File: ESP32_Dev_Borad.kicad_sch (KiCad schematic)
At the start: 33 parts, among them J1 USB_B_Micro, J2 Conn_01x19_Pin, J3 Conn_01x19_Pin, Q1 MMSS8050-H-TP, Q2 MMSS8050-H-TP, SW1 SW_Push, SW2 SW_Push, U1 CP2102N-A01-GQFN28, U2 AMS1117-3.3

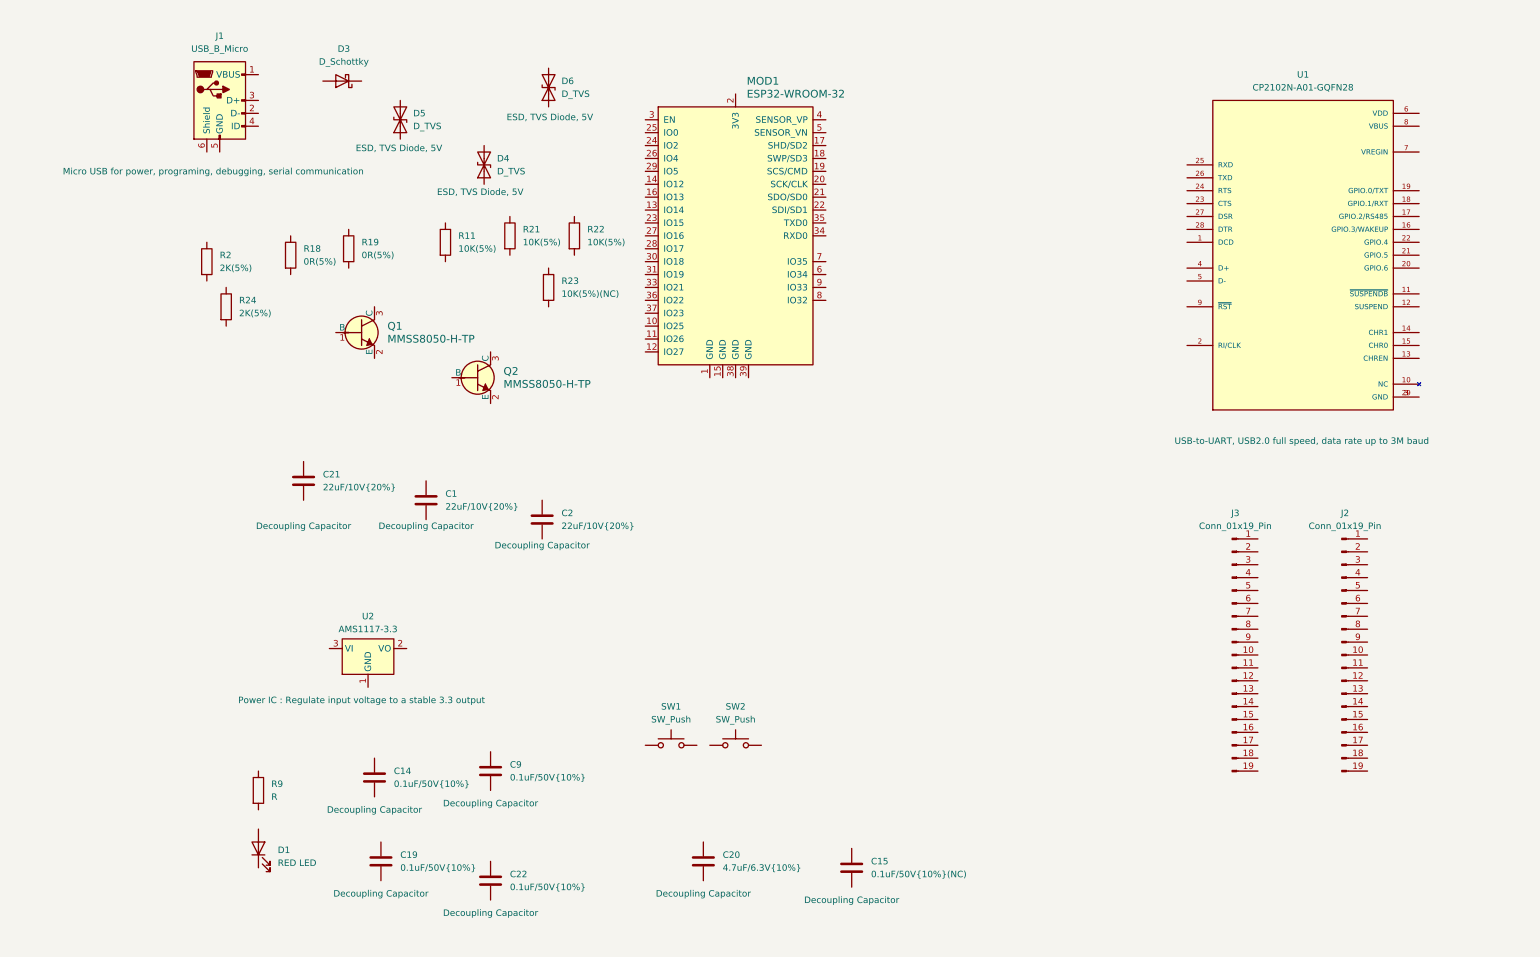
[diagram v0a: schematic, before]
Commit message: Done Arranging the schematic
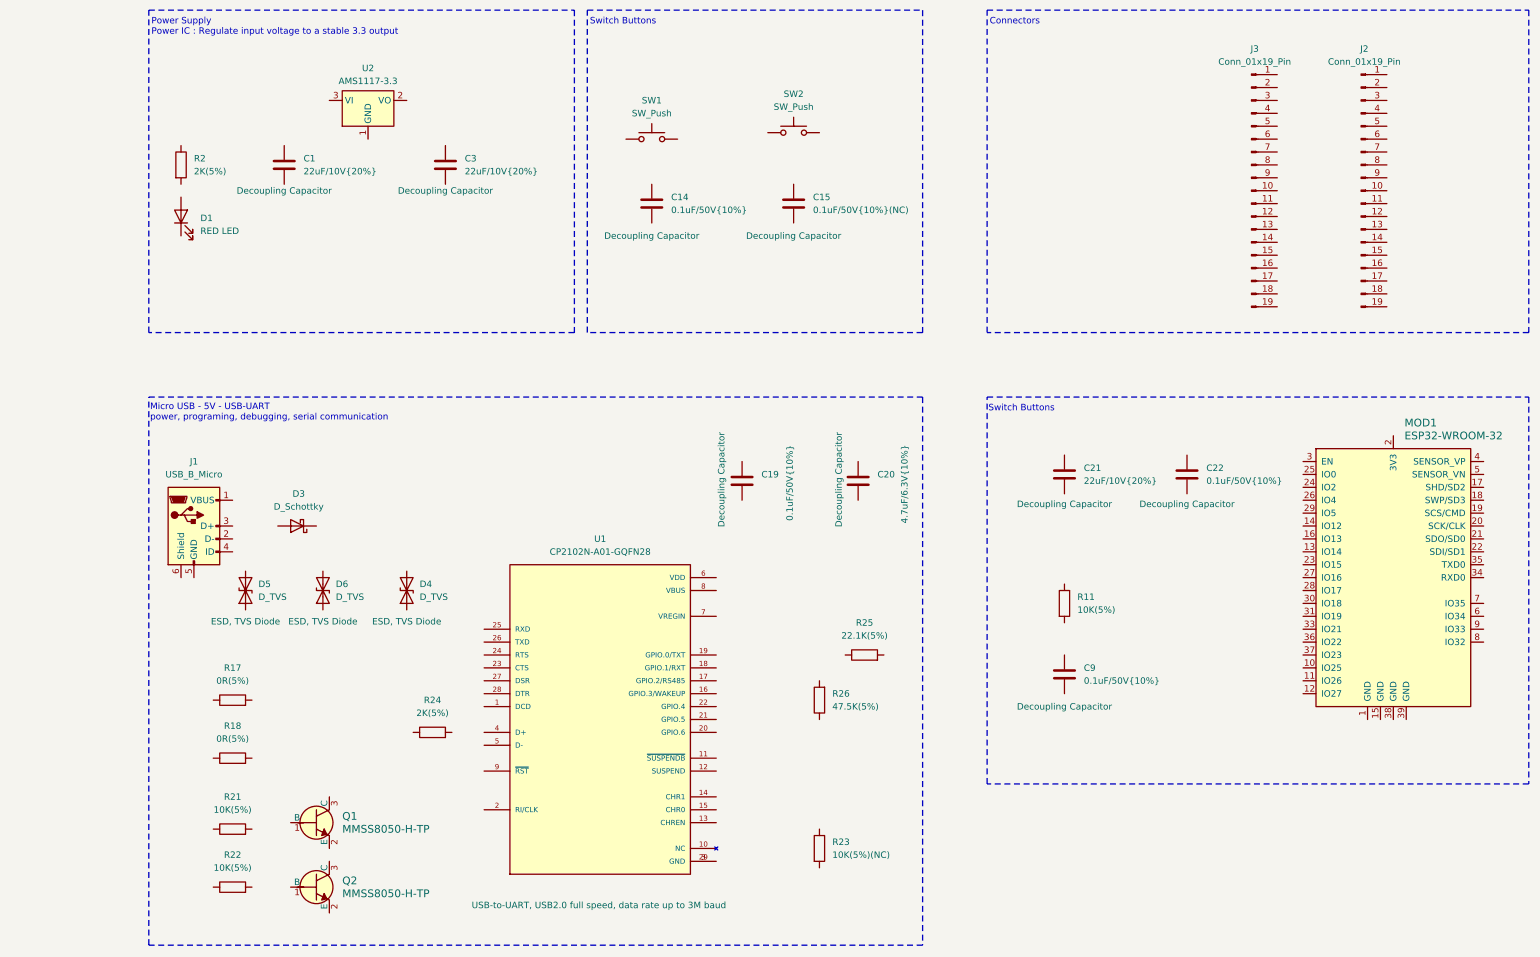
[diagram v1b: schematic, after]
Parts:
- removed R9: R, symbol Device:R
- added R25: 22.1K(5%), Resistor_SMD:R_01005_0402Metric, symbol Device:R
- added R26: 47.5K(5%), Resistor_SMD:R_01005_0402Metric, symbol Device:R
- D4, D5, D6: Purpose ESD, TVS Diode, 5V -> ESD, TVS Diode
- J1: Purpose Micro USB for power, programing, debugging, serial communic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 -> (none)
- U2: Purpose Power IC : Regulate input voltage to a stable 3.3 output -> (none)
- renumbered C2 to C3, R19 to R17
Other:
- note added: "Connectors"
- note added: "Micro USB - 5V - USB-UART power, programing, debugging, serial communication"
- note added: "Power Supply Power IC : Regulate input voltage to a stable 3.3 output"
- note added: "Switch Buttons"
- moved on the sheet: C1, C14, C15, C19, C20, C21, C22, C3, C9, D1, D3, D4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

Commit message: Done with wiring and net classes
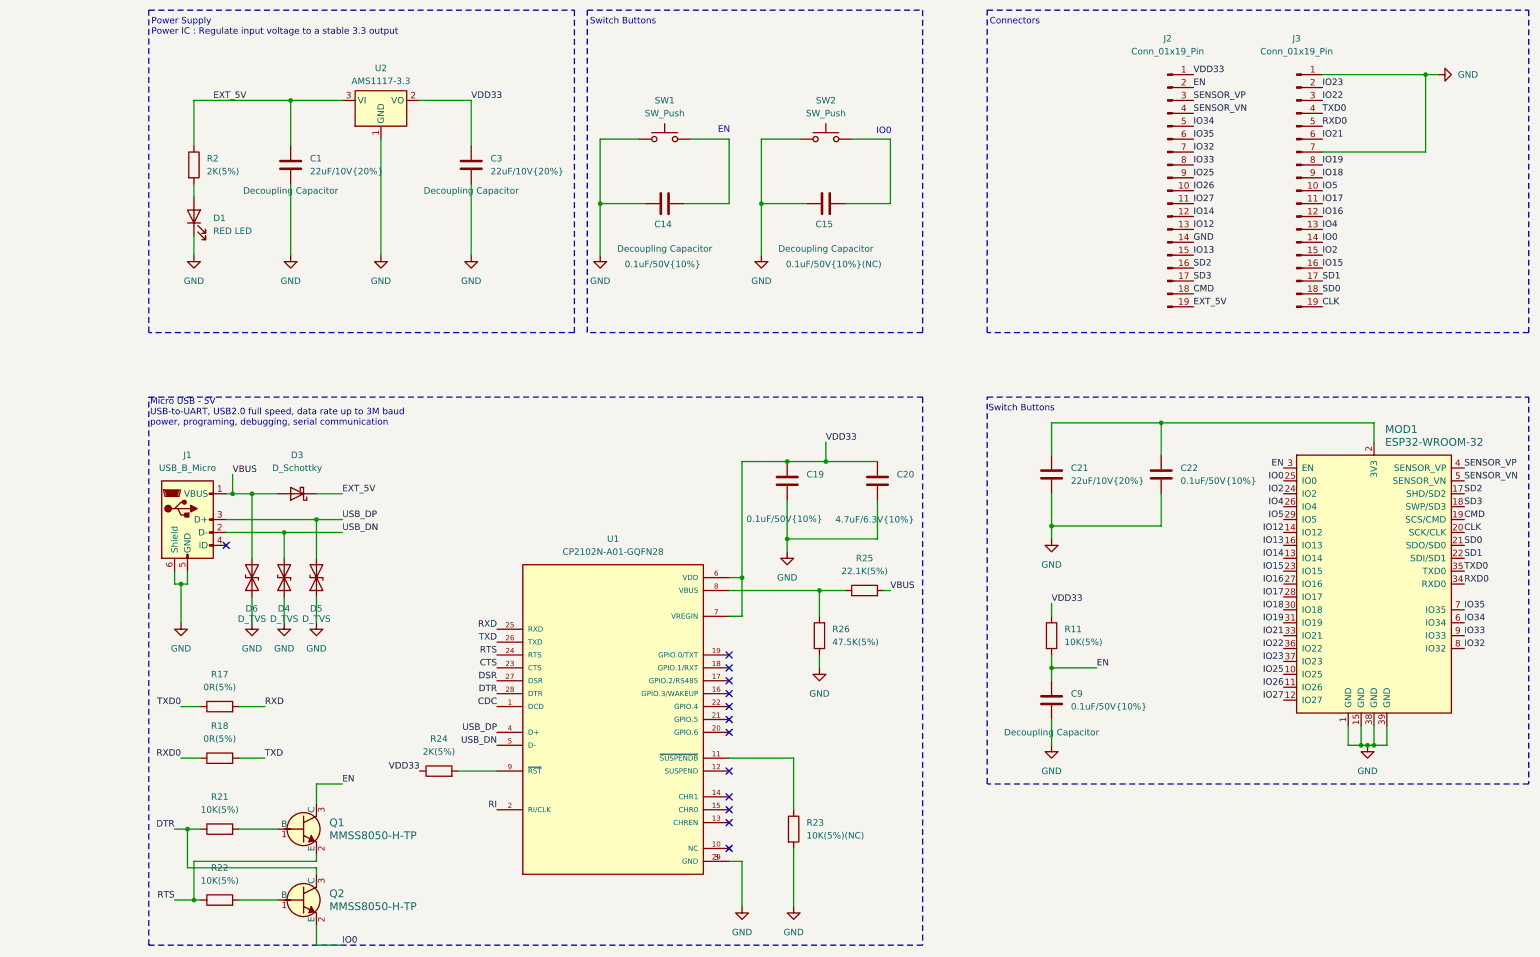
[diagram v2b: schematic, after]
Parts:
- removed J2: Conn_01x19_Pin, Connector_PinHeader_2.54mm:PinHeader_1x19_P2.54mm_Vertical, symbol Connector:Conn_01x19_Pin
- added J3: Conn_01x19_Pin, Connector_PinHeader_2.54mm:PinHeader_1x19_P2.54mm_Vertical, symbol Connector:Conn_01x19_Pin
- U1: Purpose USB-to-UART, USB2.0 full speed, data rate up to 3M baud -> (none)
- renumbered J3 to J2
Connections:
- net GND: now reaches D1.1 (K)
- net GND: now also C1.2, C14.2, C15.2, C19.2, C20.2, C21.2, C22.2, C3.2, C9.2, D4.1 (A1), D5.1 (A1), D6.1 (A1), J1.5 (GND), J1.6 (Shield), J2.14 (Pin_14), MOD1.1 (GND), MOD1.15 (GND), MOD1.38 (GND), MOD1.39 (GND), R23.2, R26.1, SW1.1, SW2.1, U1.29 (GND), U1.3 (GND), U2.1 (GND), J3.1 (Pin_1), J3.7 (Pin_7)
- net at D1.2 (A): now also R2.2
- net EXT_5V: now reaches C1.1
- net EXT_5V: now also D3.1 (K), J2.19 (Pin_19), R2.1, U2.3 (VI)
- net at C22.1: now also C21.1, MOD1.2 (3V3)
- net at SW1.2: now also C14.1
- net VDD33: now reaches J2.1 (Pin_1)
- net VDD33: now also C19.1, C20.1, C3.1, R11.1, R24.1, U1.6 (VDD), U1.7 (VREGIN), U2.2 (VO)
- net IO26: now reaches J2.10 (Pin_10)
- net IO26: now also MOD1.11 (IO26)
- net IO27: now reaches J2.11 (Pin_11)
- net IO27: now also MOD1.12 (IO27)
- net IO14: now reaches J2.12 (Pin_12)
- net IO14: now also MOD1.13 (IO14)
- net IO12: now reaches J2.13 (Pin_13)
- net IO12: now also MOD1.14 (IO12)
- net IO13: now reaches J2.15 (Pin_15)
- net IO13: now also MOD1.16 (IO13)
- net SD2: now reaches J2.16 (Pin_16)
- net SD2: now also MOD1.17 (SHD/SD2)
- net SD3: now reaches J2.17 (Pin_17)
- net SD3: now also MOD1.18 (SWP/SD3)
- net CMD: now reaches J2.18 (Pin_18)
- net CMD: now also MOD1.19 (SCS/CMD)
- net EN: now reaches J2.2 (Pin_2)
- net EN: now also C9.1, MOD1.3 (EN), Q1.3 (C), R11.2
- net SENSOR_VP: now reaches J2.3 (Pin_3)
- net SENSOR_VP: now also MOD1.4 (SENSOR_VP)
- net SENSOR_VN: now reaches J2.4 (Pin_4)
- net SENSOR_VN: now also MOD1.5 (SENSOR_VN)
- net IO34: now reaches J2.5 (Pin_5)
- net IO34: now also MOD1.6 (IO34)
- net IO35: now reaches J2.6 (Pin_6)
- net IO35: now also MOD1.7 (IO35)
- net IO32: now reaches J2.7 (Pin_7)
- net IO32: now also MOD1.8 (IO32)
- net IO33: now reaches J2.8 (Pin_8)
- net IO33: now also MOD1.9 (IO33)
- net IO25: now reaches J2.9 (Pin_9)
- net IO25: now also MOD1.10 (IO25)
- net TXD0: now reaches R17.1
- net TXD0: now also MOD1.35 (TXD0), J3.4 (Pin_4)
- net RXD: now reaches R17.2
- net RXD: now also U1.25 (RXD)
- net DTR: now reaches R21.1
- net DTR: now also Q2.3 (C), U1.28 (DTR)
- net at R21.2: now also Q1.1 (B)
- net at R23.1: now also U1.11 (~{SUSPENDB})
- net RXD0: now reaches R18.1
- net RXD0: now also MOD1.34 (RXD0), J3.5 (Pin_5)
- net TXD: now reaches R18.2
- net TXD: now also U1.26 (TXD)
- net VBUS: now reaches J1.1 (VBUS)
- net VBUS: now also D3.2 (A), D6.2 (A2), R25.2
- net USB_DN: now reaches J1.2 (D-)
- net USB_DN: now also D4.2 (A2), U1.5 (D-)
- net USB_DP: now reaches J1.3 (D+)
- net USB_DP: now also D5.2 (A2), U1.4 (D+)
- net at R24.2: now also U1.9 (~{RST})
- net CLK: now reaches MOD1.20 (SCK/CLK)
- net CLK: now also J3.19 (Pin_19)
- net SD0: now reaches MOD1.21 (SDO/SD0)
- net SD0: now also J3.18 (Pin_18)
- net SD1: now reaches MOD1.22 (SDI/SD1)
- net SD1: now also J3.17 (Pin_17)
- net IO15: now reaches MOD1.23 (IO15)
- net IO15: now also J3.16 (Pin_16)
- net IO2: now reaches MOD1.24 (IO2)
- net IO2: now also J3.15 (Pin_15)
- net IO0: now reaches MOD1.25 (IO0)
- net IO0: now also Q2.2 (E), J3.14 (Pin_14)
- net IO4: now reaches MOD1.26 (IO4)
- net IO4: now also J3.13 (Pin_13)
- net IO16: now reaches MOD1.27 (IO16)
- net IO16: now also J3.12 (Pin_12)
- net IO17: now reaches MOD1.28 (IO17)
- net IO17: now also J3.11 (Pin_11)
- net IO5: now reaches MOD1.29 (IO5)
- net IO5: now also J3.10 (Pin_10)
- net IO18: now reaches MOD1.30 (IO18)
- net IO18: now also J3.9 (Pin_9)
- net IO19: now reaches MOD1.31 (IO19)
- net IO19: now also J3.8 (Pin_8)
- net IO21: now reaches MOD1.33 (IO21)
- net IO21: now also J3.6 (Pin_6)
- net IO22: now reaches MOD1.36 (IO22)
- net IO22: now also J3.3 (Pin_3)
- net IO23: now reaches MOD1.37 (IO23)
- net IO23: now also J3.2 (Pin_2)
- net CDC: now reaches U1.1 (DCD)
- net RI: now reaches U1.2 (RI/CLK)
- net CTS: now reaches U1.23 (CTS)
- net RTS: now reaches U1.24 (RTS)
- net RTS: now also Q1.2 (E), R22.1
- net DSR: now reaches U1.27 (DSR)
- net at U1.8 (VBUS): now also R25.1, R26.2
- net at R22.2: now also Q2.1 (B)
- net at C15.1: now also SW2.2
- no-connect marks 0 -> 13
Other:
- note added: "EN"
- note added: "IO0"
- note added: "Micro USB - 5V USB-to-UART, USB2.0 full speed, data rate up to 3M baud power, programing, debugging, serial communication"
- note removed: "Micro USB - 5V - USB-UART power, programing, debugging, serial communication"
- company: (none) -> Majed Dev
- moved on the sheet: C1, C14, C19, C20, C21, C22, C3, C9, D1, D3, D6, J1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

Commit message: Done with schematic
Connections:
- net CDC renamed DCD
- no-connect marks 13 -> 12
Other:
- note added: "Auto Program DRT RTS --> EN IO0 1 1 1 1 0 0 1 1 1 0 0 1 0 1 1 0"
- moved on the sheet: Q1, Q2
